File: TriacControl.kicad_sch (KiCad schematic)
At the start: 55 parts, among them J1 AC LINE, J2 LOAD, J3 ZEROCROSS, J4 PWM, Q1 BT136-600, Q2 2N3906, U1 MOC3020M, U2 PC817, U3 PC817

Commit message: A few changes
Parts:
- added R27: 2k2, Resistor_THT:R_Axial_DIN0207_L6.3mm_D2.5mm_P7.62mm_Horizontal, symbol Device:R
- Q2: value 2N3906 -> 2N2907
- R23, R24: value 100R -> 10R
- R25: value 10k -> 220R
- R26: value 22k -> 2k2
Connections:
- net at D2.2 (A), D4.1 (K), R4.1: now also R27.2
- net at D1.2 (A), D3.1 (K), R5.1: now also R27.1
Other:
- note added: "R26 is 2k2 for 120 VAC R26 is 1k for 220 VAC"
- note added: "R27 is 2k2 for 120 VAC R27 is 1k for 220 VAC"
- moved on the sheet: R4, R5
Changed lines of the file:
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@@
   (junction (at 199.39 71.755) (diameter 0) (color 0 0 0 0)
   )
+  (junction (at 184.15 75.565) (diameter 0) (color 0 0 0 0)
+  )
   (junction (at 152.4 132.08) (diameter 0) (color 0 0 0 0)
   )
@@
   (junction (at 114.935 69.85) (diameter 0) (color 0 0 0 0)
   )
+  (junction (at 199.39 75.565) (diameter 0) (color 0 0 0 0)
+  )
   (junction (at 184.15 71.755) (diameter 0) (color 0 0 0 0)
   )
@@
     (stroke (width 0) (type default))
   )
+  (wire (pts (xy 194.945 75.565) (xy 199.39 75.565))
+    (stroke (width 0) (type default))
+  )
   (wire (pts (xy 102.87 83.82) (xy 104.14 83.82))
     (stroke (width 0) (type default))
@@
     (stroke (width 0) (type default))
   )
-  (wire (pts (xy 199.39 71.755) (xy 199.39 74.93))
+  (wire (pts (xy 199.39 71.755) (xy 199.39 75.565))
     (stroke (width 0) (type default))
   )
@@
     (stroke (width 0) (type default))
   )
+  (wire (pts (xy 199.39 75.565) (xy 199.39 76.835))
+    (stroke (width 0) (type default))
+  )
   (wire (pts (xy 168.91 95.885) (xy 165.735 95.885))
     (stroke (width 0) (type default))
@@
     (stroke (width 0) (type default))
   )
+  (wire (pts (xy 184.15 75.565) (xy 187.325 75.565))
+    (stroke (width 0) (type default))
+  )
   (wire (pts (xy 139.065 124.46) (xy 133.35 124.46))
     (stroke (width 0) (type default))
@@
     (stroke (width 0) (type default))
   )
-  (wire (pts (xy 199.39 82.55) (xy 199.39 85.09))
+  (wire (pts (xy 199.39 84.455) (xy 199.39 85.09))
     (stroke (width 0) (type default))
   )
@@
     (stroke (width 0) (type default))
   )
-  (wire (pts (xy 184.15 82.55) (xy 184.15 85.09))
+  (wire (pts (xy 184.15 84.455) (xy 184.15 85.09))
     (stroke (width 0) (type default))
   )
@@
     (stroke (width 0) (type default))
   )
+  (wire (pts (xy 184.15 75.565) (xy 184.15 71.755))
+    (stroke (width 0) (type default))
+  )
   (wire (pts (xy 157.48 124.46) (xy 162.56 124.46))
     (stroke (width 0) (type default))
@@
     (stroke (width 0) (type default))
   )
-  (wire (pts (xy 184.15 74.93) (xy 184.15 71.755))
+  (wire (pts (xy 184.15 76.835) (xy 184.15 75.565))
     (stroke (width 0) (type default))
   )
@@
   (wire (pts (xy 113.03 102.235) (xy 113.03 103.505))
     (stroke (width 0) (type default))
+  )
+  (text "R26 is 2k2 for 120 VAC\nR26 is 1k for 220 VAC" (at 151.765 104.14 0)
+    (effects (font (size 1.27 1.27)) (justify left bottom))
   )
   (text "LOADNEUTRAL" (at 204.47 141.605 0)
     (effects (font (size 1.27 1.27)) (justify left bottom))
   )
+  (text "R27 is 2k2 for 120 VAC\nR27 is 1k for 220 VAC" (at 205.74 75.565 0)
+    (effects (font (size 1.27 1.27)) (justify left bottom))
+  )
   (text "NEUTRAL" (at 205.105 123.19 0)
     (effects (font (size 1.27 1.27)) (justify left bottom))
@@
       (effects (font (size 1.27 1.27)) (justify left))
     )
-    (property "Value" "10k" (at 144.78 86.995 90)
+    (property "Value" "220R" (at 146.05 86.995 90)
       (effects (font (size 1.27 1.27)) (justify left))
     )
@@
       (effects (font (size 1.27 1.27)) (justify left))
     )
-    (property "Value" "100R" (at 132.715 90.805 90)
+    (property "Value" "10R" (at 132.715 90.805 90)
       (effects (font (size 1.27 1.27)) (justify left))
     )
@@
     )
   )
-  (symbol (lib_id "Device:R") (at 199.39 78.74 0) (unit 1)
-    (in_bom yes) (on_board yes) (dnp no)
-    (property "Reference" "R4" (at 194.945 77.47 0)
-      (effects (font (size 1.27 1.27)) (justify left))
-    )
-    (property "Value" "10k" (at 199.39 81.28 90)
-      (effects (font (size 1.27 1.27)) (justify left))
-    )
-    (property "Footprint" "Resistor_THT:R_Axial_DIN0207_L6.3mm_D2.5mm_P7.62mm_Horizontal" (at 197.612 78.74 90)
-      (effects (font (size 1.27 1.27)) hide)
-    )
-    (property "Datasheet" "~" (at 199.39 78.74 0)
+  (symbol (lib_id "Device:R") (at 199.39 80.645 0) (unit 1)
+    (in_bom yes) (on_board yes) (dnp no)
+    (property "Reference" "R4" (at 194.945 79.375 0)
+      (effects (font (size 1.27 1.27)) (justify left))
+    )
+    (property "Value" "10k" (at 199.39 83.185 90)
+      (effects (font (size 1.27 1.27)) (justify left))
+    )
+    (property "Footprint" "Resistor_THT:R_Axial_DIN0207_L6.3mm_D2.5mm_P7.62mm_Horizontal" (at 197.612 80.645 90)
+      (effects (font (size 1.27 1.27)) hide)
+    )
+    (property "Datasheet" "~" (at 199.39 80.645 0)
       (effects (font (size 1.27 1.27)) hide)
     )
@@
       (effects (font (size 1.27 1.27)) (justify left))
     )
-    (property "Value" "2N3906" (at 145.415 91.44 0)
+    (property "Value" "2N2907" (at 145.415 91.44 0)
       (effects (font (size 1.27 1.27)) (justify left))
     )
@@
     )
   )
+  (symbol (lib_id "Device:R") (at 191.135 75.565 90) (unit 1)
+    (in_bom yes) (on_board yes) (dnp no)
+    (property "Reference" "R27" (at 193.04 78.105 90)
+      (effects (font (size 1.27 1.27)) (justify left))
+    )
+    (property "Value" "2k2" (at 193.675 75.565 90)
+      (effects (font (size 1.27 1.27)) (justify left))
+    )
+    (property "Footprint" "Resistor_THT:R_Axial_DIN0207_L6.3mm_D2.5mm_P7.62mm_Horizontal" (at 191.135 77.343 90)
+      (effects (font (size 1.27 1.27)) hide)
+    )
+    (property "Datasheet" "~" (at 191.135 75.565 0)
+      (effects (font (size 1.27 1.27)) hide)
+    )
+    (pin "1")
+    (pin "2")
+    (instances
+      (project "TriacControl"
+        (path "/1a4acada-7416-4f16-a08a-34e040185620"
+          (reference "R27") (unit 1)
+        )
+      )
+    )
+  )
   (symbol (lib_id "Device:R") (at 145.415 59.055 0) (unit 1)
     (in_bom yes) (on_board yes) (dnp no)
@@
       (effects (font (size 1.27 1.27)) (justify left))
     )
-    (property "Value" "22k" (at 144.78 100.965 90)
+    (property "Value" "2k2" (at 144.78 100.965 90)
       (effects (font (size 1.27 1.27)) (justify left))
     )
@@
     )
   )
-  (symbol (lib_id "Device:R") (at 184.15 78.74 0) (unit 1)
-    (in_bom yes) (on_board yes) (dnp no)
-    (property "Reference" "R5" (at 179.705 77.47 0)
-      (effects (font (size 1.27 1.27)) (justify left))
-    )
-    (property "Value" "10k" (at 184.15 81.28 90)
-      (effects (font (size 1.27 1.27)) (justify left))
-    )
-    (property "Footprint" "Resistor_THT:R_Axial_DIN0207_L6.3mm_D2.5mm_P7.62mm_Horizontal" (at 182.372 78.74 90)
-      (effects (font (size 1.27 1.27)) hide)
-    )
-    (property "Datasheet" "~" (at 184.15 78.74 0)
+  (symbol (lib_id "Device:R") (at 184.15 80.645 0) (unit 1)
+    (in_bom yes) (on_board yes) (dnp no)
+    (property "Reference" "R5" (at 179.705 79.375 0)
+      (effects (font (size 1.27 1.27)) (justify left))
+    )
+    (property "Value" "10k" (at 184.15 83.185 90)
+      (effects (font (size 1.27 1.27)) (justify left))
+    )
+    (property "Footprint" "Resistor_THT:R_Axial_DIN0207_L6.3mm_D2.5mm_P7.62mm_Horizontal" (at 182.372 80.645 90)
+      (effects (font (size 1.27 1.27)) hide)
+    )
+    (property "Datasheet" "~" (at 184.15 80.645 0)
       (effects (font (size 1.27 1.27)) hide)
     )
@@
       (effects (font (size 1.27 1.27)) (justify left))
     )
-    (property "Value" "100R" (at 107.95 124.46 90)
-      (effects (font (size 1.27 1.27)) (justify left))
-    )
+    (property "Value" "10R" (at 107.95 124.46 90)
+      (effects (font (size 1.27 1.27)) (justify left))
+    )

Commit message: Changed values, moved parts
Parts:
- C2: value 100 uF -> 47 uF
- C3: value 47 uF -> 22 uF
- C4: value 22 uF -> 10 uF
- R17, R18: value 1k -> 3k3
- R19: value 1k -> 820R
- R20: value 1k -> 330R
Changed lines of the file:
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@@
       (effects (font (size 1.27 1.27)) (justify left))
     )
-    (property "Value" "22 uF" (at 127 106.7689 0)
+    (property "Value" "10 uF" (at 127 106.7689 0)
       (effects (font (size 1.27 1.27)) (justify left))
     )
@@
       (effects (font (size 1.27 1.27)) (justify left))
     )
-    (property "Value" "1k" (at 100.457 83.693 90)
+    (property "Value" "330R" (at 101.6 83.82 90)
       (effects (font (size 1.27 1.27)) (justify left))
     )
@@
       (effects (font (size 1.27 1.27)) (justify left))
     )
-    (property "Value" "1k" (at 100.457 62.738 90)
+    (property "Value" "3k3" (at 100.965 62.865 90)
       (effects (font (size 1.27 1.27)) (justify left))
     )
@@
       (effects (font (size 1.27 1.27)) (justify left))
     )
-    (property "Value" "100 uF" (at 104.14 107.4039 0)
+    (property "Value" "47 uF" (at 104.14 107.4039 0)
       (effects (font (size 1.27 1.27)) (justify left))
     )
@@
       (effects (font (size 1.27 1.27)) (justify left))
     )
-    (property "Value" "1k" (at 100.457 69.723 90)
+    (property "Value" "3k3" (at 100.965 69.85 90)
       (effects (font (size 1.27 1.27)) (justify left))
     )
@@
       (effects (font (size 1.27 1.27)) (justify left))
     )
-    (property "Value" "1k" (at 100.457 76.708 90)
+    (property "Value" "820R" (at 101.6 76.835 90)
       (effects (font (size 1.27 1.27)) (justify left))
     )
@@
       (effects (font (size 1.27 1.27)) (justify left))
     )
-    (property "Value" "47 uF" (at 115.57 106.7689 0)
-      (effects (font (size 1.27 1.27)) (justify left))
-    )
+    (property "Value" "22 uF" (at 115.57 106.7689 0)
+      (effects (font (size 1.27 1.27)) (justify left))
+    )

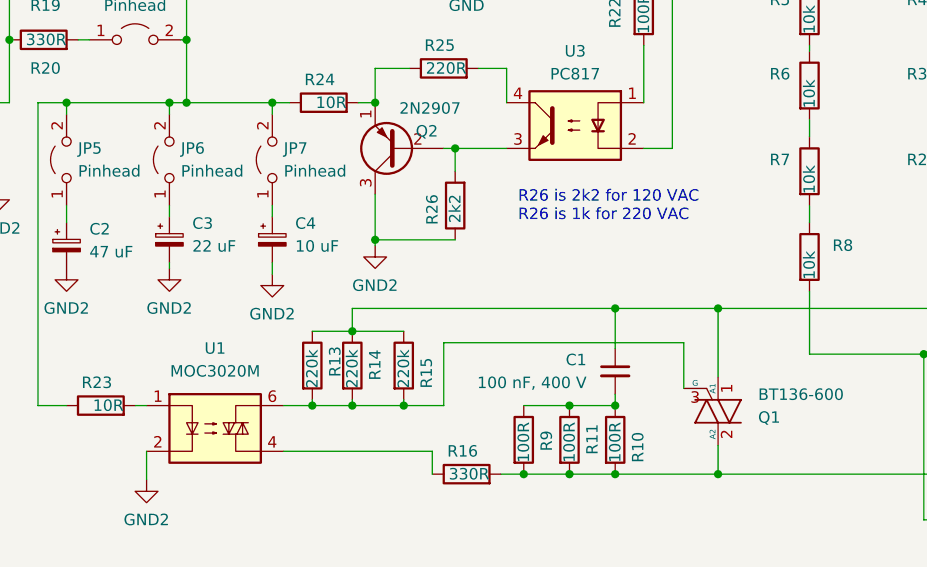
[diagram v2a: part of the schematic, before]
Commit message: Fixed names and traces
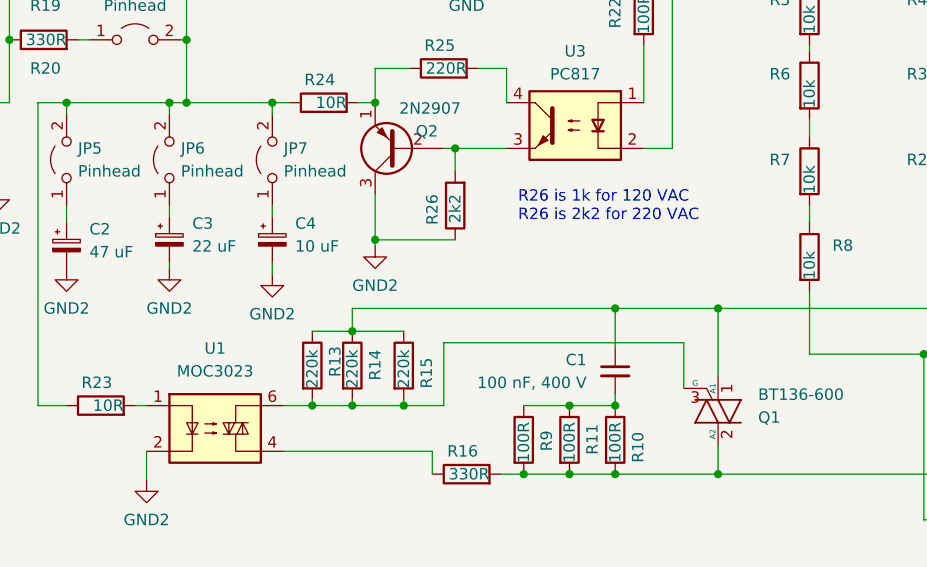
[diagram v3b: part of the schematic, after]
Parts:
- U1: value MOC3020M -> MOC3023
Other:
- note added: "R26 is 1k for 120 VAC R26 is 2k2 for 220 VAC"
- note removed: "R26 is 2k2 for 120 VAC R26 is 1k for 220 VAC"
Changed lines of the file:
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@@
     (stroke (width 0) (type default))
   )
-  (text "R26 is 2k2 for 120 VAC\nR26 is 1k for 220 VAC" (at 151.765 104.14 0)
+  (text "R26 is 1k for 120 VAC\nR26 is 2k2 for 220 VAC" (at 151.765 104.14 0)
     (effects (font (size 1.27 1.27)) (justify left bottom))
   )
@@
       (effects (font (size 1.27 1.27)))
     )
-    (property "Value" "MOC3020M" (at 118.11 120.65 0)
-      (effects (font (size 1.27 1.27)))
-    )
+    (property "Value" "MOC3023" (at 118.11 120.65 0)
+      (effects (font (size 1.27 1.27)))
+    )

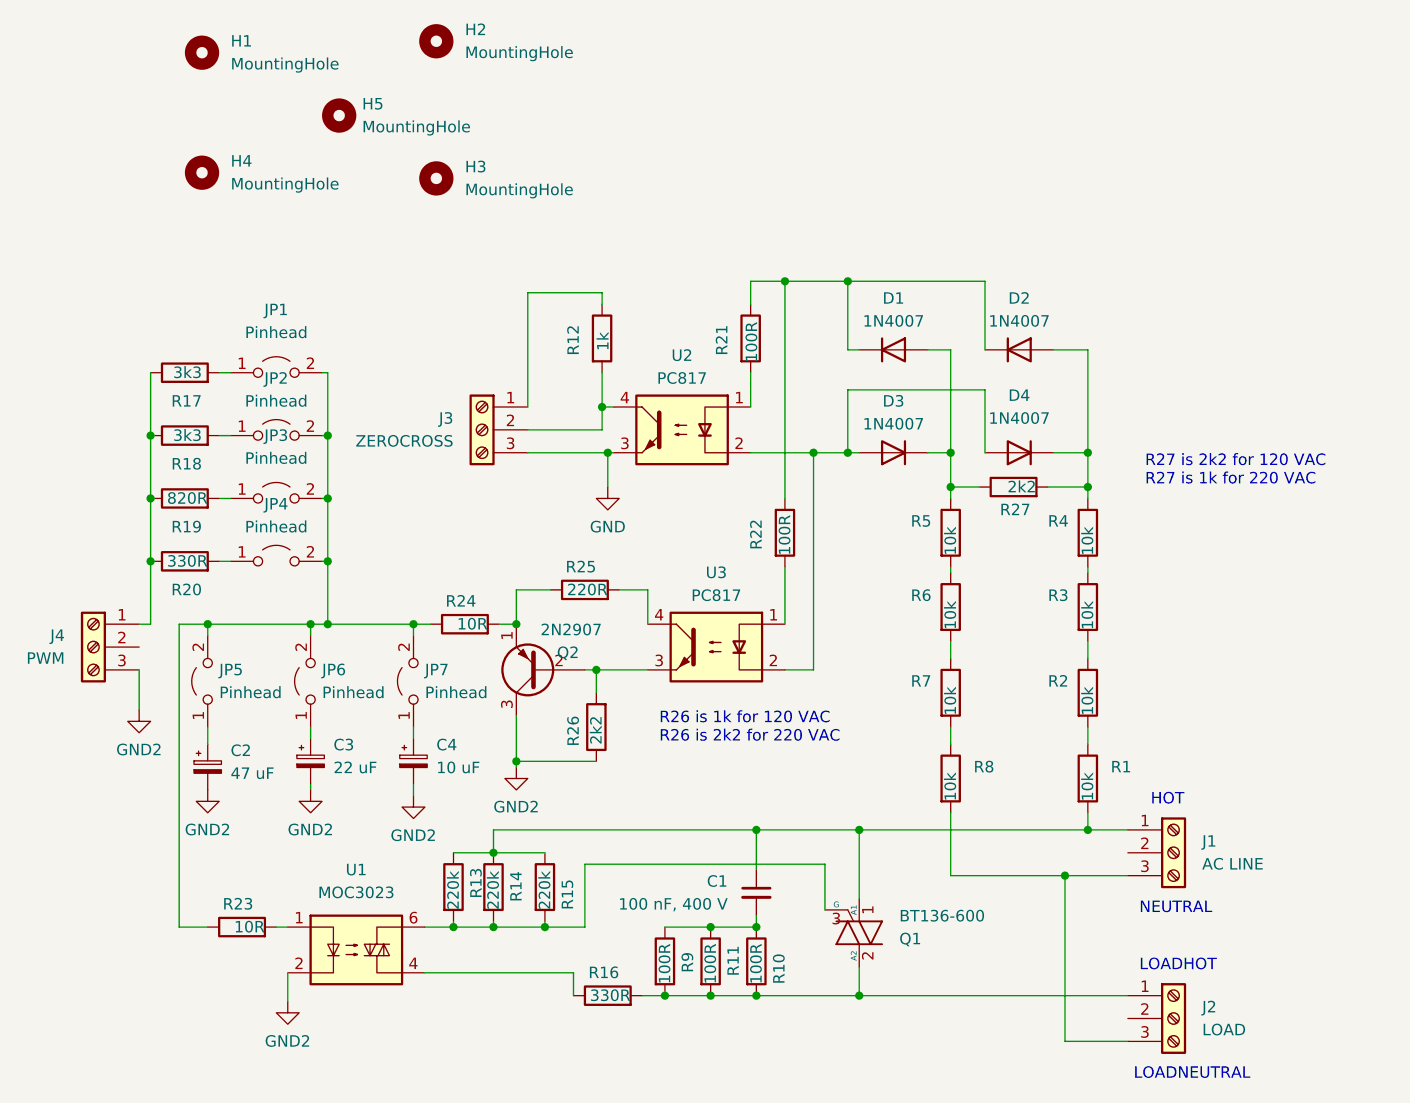
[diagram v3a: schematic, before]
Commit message: Changed connection to snubber, resistor size, etc.
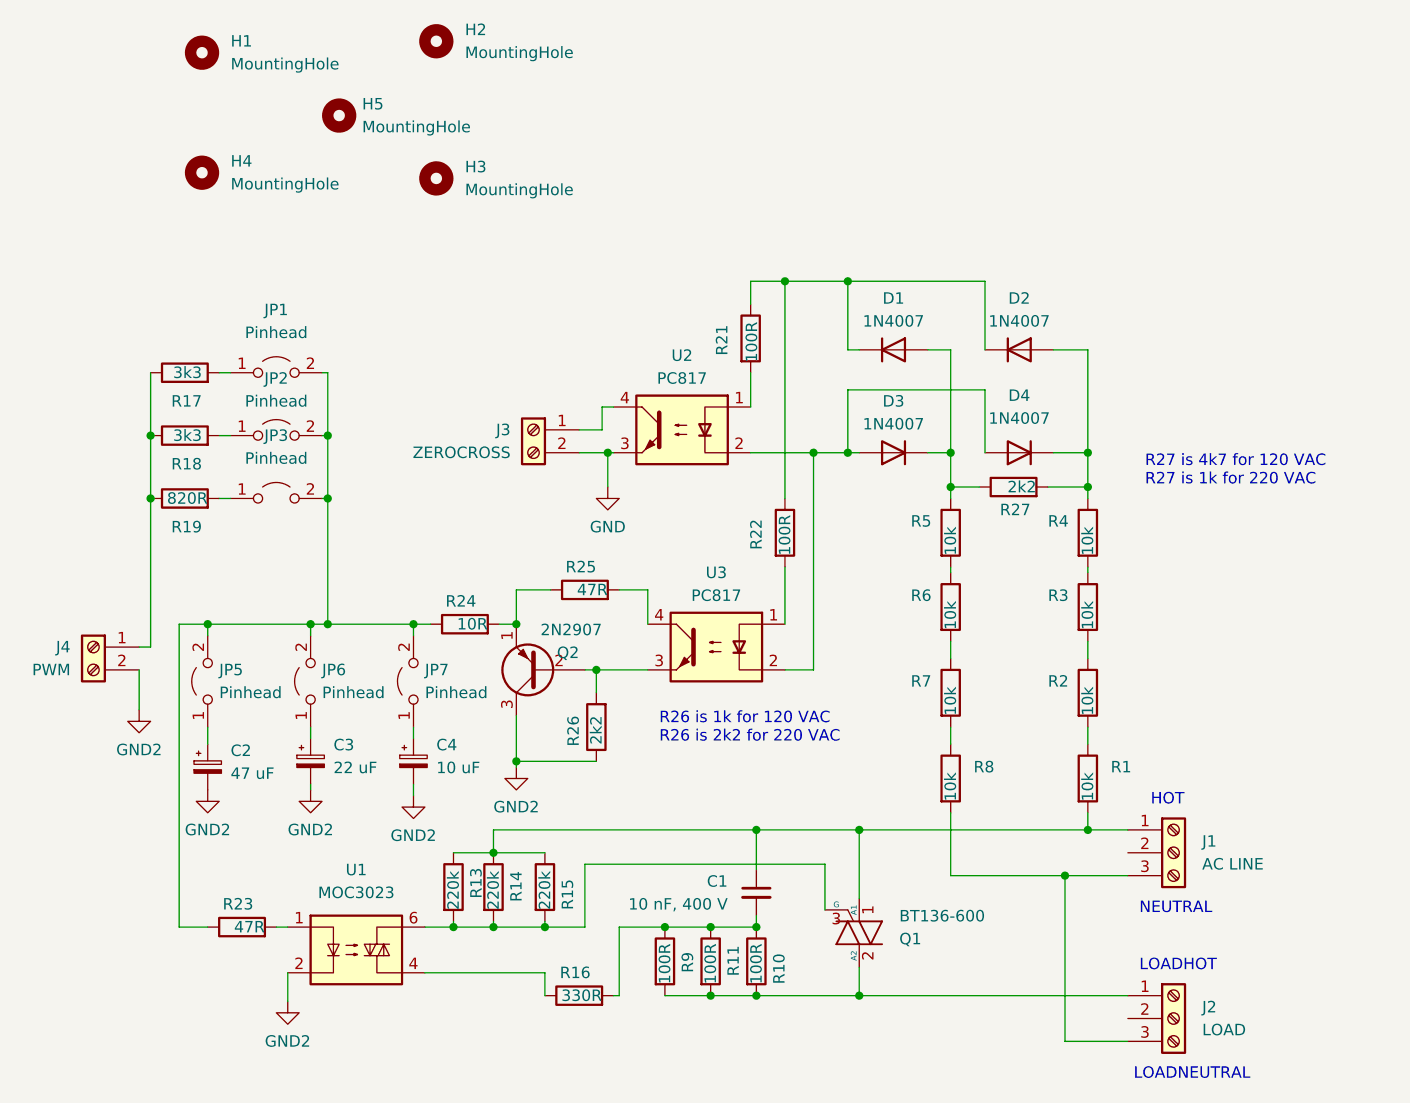
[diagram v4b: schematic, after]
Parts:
- removed J3: ZEROCROSS, TerminalBlock:TerminalBlock_bornier-3_P5.08mm, symbol Connector:Screw_Terminal_01x03
- removed J4: PWM, TerminalBlock:TerminalBlock_bornier-3_P5.08mm, symbol Connector:Screw_Terminal_01x03
- removed JP4: Pinhead, Connector_PinHeader_2.54mm:PinHeader_1x02_P2.54mm_Vertical, symbol Jumper:Jumper_2_Open
- removed R12: 1k, Resistor_THT:R_Axial_DIN0207_L6.3mm_D2.5mm_P7.62mm_Horizontal, symbol Device:R
- removed R20: 330R, Resistor_THT:R_Axial_DIN0207_L6.3mm_D2.5mm_P7.62mm_Horizontal, symbol Device:R
- added J3: ZEROCROSS, TerminalBlock:TerminalBlock_bornier-2_P5.08mm, symbol Connector:Screw_Terminal_01x02
- added J4: PWM, TerminalBlock:TerminalBlock_bornier-2_P5.08mm, symbol Connector:Screw_Terminal_01x02
- C1: value 100 nF, 400 V -> 10 nF, 400 V
- R17, R18, R19: footprint Resistor_THT:R_Axial_DIN0207_L6.3mm_D2.5mm_P7.62mm_Horizontal -> Resistor_THT:R_Axial_DIN0309_L9.0mm_D3.2mm_P15.24mm_Horizontal
- R23: value 10R -> 47R
- R25: value 220R -> 47R
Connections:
- net GND: now also J3.2 (Pin_2)
- net GND2: now also J4.2 (Pin_2)
- net at C1.2, R10.1, R11.1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: now also R16.2
- net at J2.1 (Pin_1), Q1.2 (A2), R10.2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: no longer R16.2
- net at U2.4: now also J3.1 (Pin_1)
- net at R17.1, R18.1, R19.1: now also J4.1 (Pin_1)
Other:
- note added: "R27 is 4k7 for 120 VAC R27 is 1k for 220 VAC"
- note removed: "R27 is 2k2 for 120 VAC R27 is 1k for 220 VAC"
- moved on the sheet: R16

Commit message: Fixed positioning of component
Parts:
- R24: value 10R -> 4R7
- R26: value 2k2 -> 1k
- R27: value 2k2 -> 4k7
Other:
- note added: "R27 is 4k7 for 120 VAC R27 is 2k2 for 220 VAC"
- note removed: "R26 is 1k for 120 VAC R26 is 2k2 for 220 VAC"
- note removed: "R27 is 4k7 for 120 VAC R27 is 1k for 220 VAC"
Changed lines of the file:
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@@
     (stroke (width 0) (type default))
-  )
-  (text "R26 is 1k for 120 VAC\nR26 is 2k2 for 220 VAC" (at 151.765 104.14 0)
-    (effects (font (size 1.27 1.27)) (justify left bottom))
   )
   (text "LOADNEUTRAL" (at 204.47 141.605 0)
     (effects (font (size 1.27 1.27)) (justify left bottom))
   )
-  (text "R27 is 4k7 for 120 VAC\nR27 is 1k for 220 VAC" (at 205.74 75.565 0)
+  (text "R27 is 4k7 for 120 VAC\nR27 is 2k2 for 220 VAC" (at 205.74 75.565 0)
     (effects (font (size 1.27 1.27)) (justify left bottom))
   )
@@
       (effects (font (size 1.27 1.27)) (justify left))
     )
-    (property "Value" "10R" (at 132.715 90.805 90)
+    (property "Value" "4R7" (at 132.715 90.805 90)
       (effects (font (size 1.27 1.27)) (justify left))
     )
@@
       (effects (font (size 1.27 1.27)) (justify left))
     )
-    (property "Value" "2k2" (at 193.675 75.565 90)
+    (property "Value" "4k7" (at 193.675 75.565 90)
       (effects (font (size 1.27 1.27)) (justify left))
     )
@@
       (effects (font (size 1.27 1.27)) (justify left))
     )
-    (property "Value" "2k2" (at 144.78 100.965 90)
-      (effects (font (size 1.27 1.27)) (justify left))
-    )
+    (property "Value" "1k" (at 144.78 100.965 90)
+      (effects (font (size 1.27 1.27)) (justify left))
+    )

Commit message: Moved snubber capacitor
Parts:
- Q1: value BT136-600 -> BTA16-600
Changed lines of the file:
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@@
       (effects (font (size 1.27 1.27)) (justify left))
     )
-    (property "Value" "BT136-600" (at 178.435 123.2408 0)
+    (property "Value" "BTA16-600" (at 178.435 123.2408 0)
       (effects (font (size 1.27 1.27)) (justify left))
     )

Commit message: Moved components a little ore
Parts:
- C1: footprint Capacitor_THT:C_Disc_D5.0mm_W2.5mm_P5.00mm -> Capacitor_THT:C_Rect_L10.0mm_W2.5mm_P7.50mm_MKS4
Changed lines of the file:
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@@
       (effects (font (size 1.27 1.27)) (justify left))
     )
-    (property "Footprint" "Capacitor_THT:C_Disc_D5.0mm_W2.5mm_P5.00mm" (at 162.56 120.65 0)
+    (property "Footprint" "Capacitor_THT:C_Rect_L10.0mm_W2.5mm_P7.50mm_MKS4" (at 162.56 120.65 0)
       (effects (font (size 1.27 1.27)) hide)
     )
